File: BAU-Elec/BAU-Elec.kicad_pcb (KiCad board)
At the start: 2 copper layers, 47.7 x 36.7 mm, 18 parts, among them K1 G2RL-1-E, P16NF06L1 P16NF06L, U2 74LS04

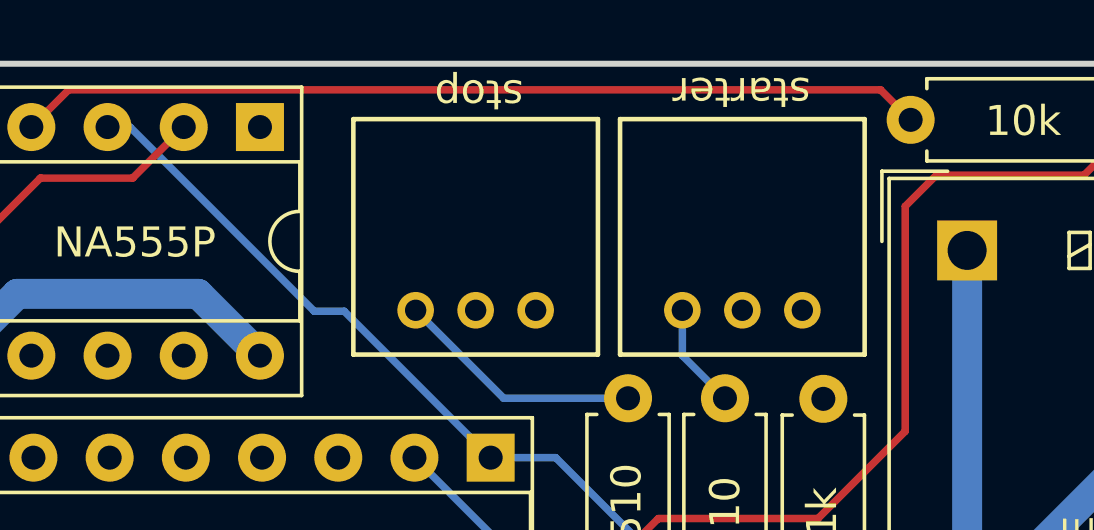
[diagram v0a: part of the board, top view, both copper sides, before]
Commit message: Fix: missing wires
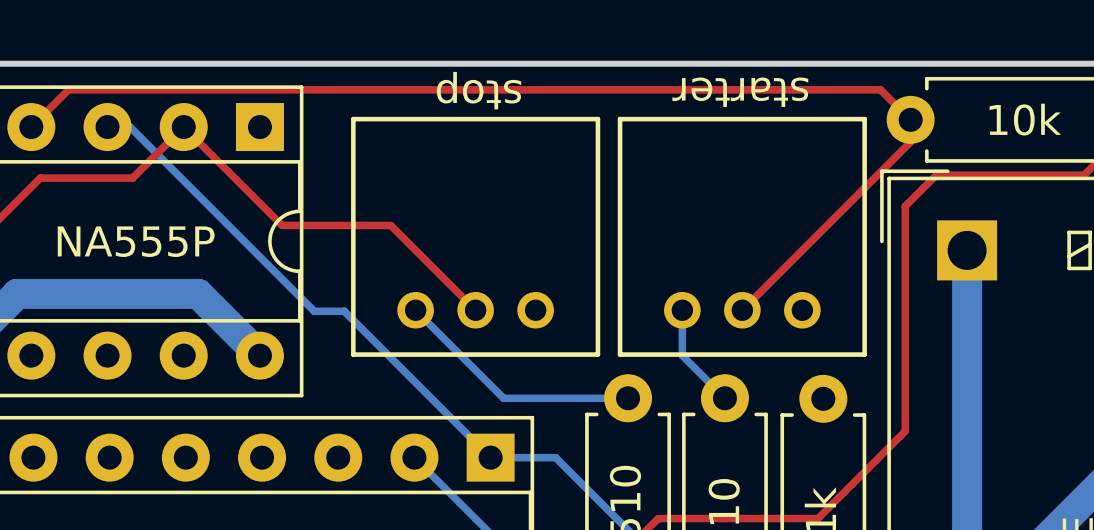
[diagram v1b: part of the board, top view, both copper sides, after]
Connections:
- NA555P1 pad 2: Net-(NA555P1-TR) -> stop_button
- NA555P1 pad 4: Net-(NA555P1-R) -> primer_button
- R1 pad 2: Net-(NA555P1-TR) -> stop_button
- R2 pad 2: Net-(NA555P1-R) -> primer_button
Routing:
- net stop_button: track 0.00 -> 81.7 mm
- net Net-(NA555P1-TR): track 69.5 -> 0.00 mm
- net primer_button: track 0.00 -> 38.9 mm
- net Net-(NA555P1-R): track 30.2 -> 0.00 mm
